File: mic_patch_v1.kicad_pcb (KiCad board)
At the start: 4 copper layers, 40 x 31 mm, 54 parts, among them J1 Conn_ARM_SWD_TagConnect_TC203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, J2 J_000002, J3 J_000001, J4 Micro_SD_Card, J5 J_000003, SW1 SW_000001, SW2 SW_000001, U1 NORA-B106-00B, U2 PWR_nPM1100-QDXX, U3 ADAU7002ACBZ-R7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

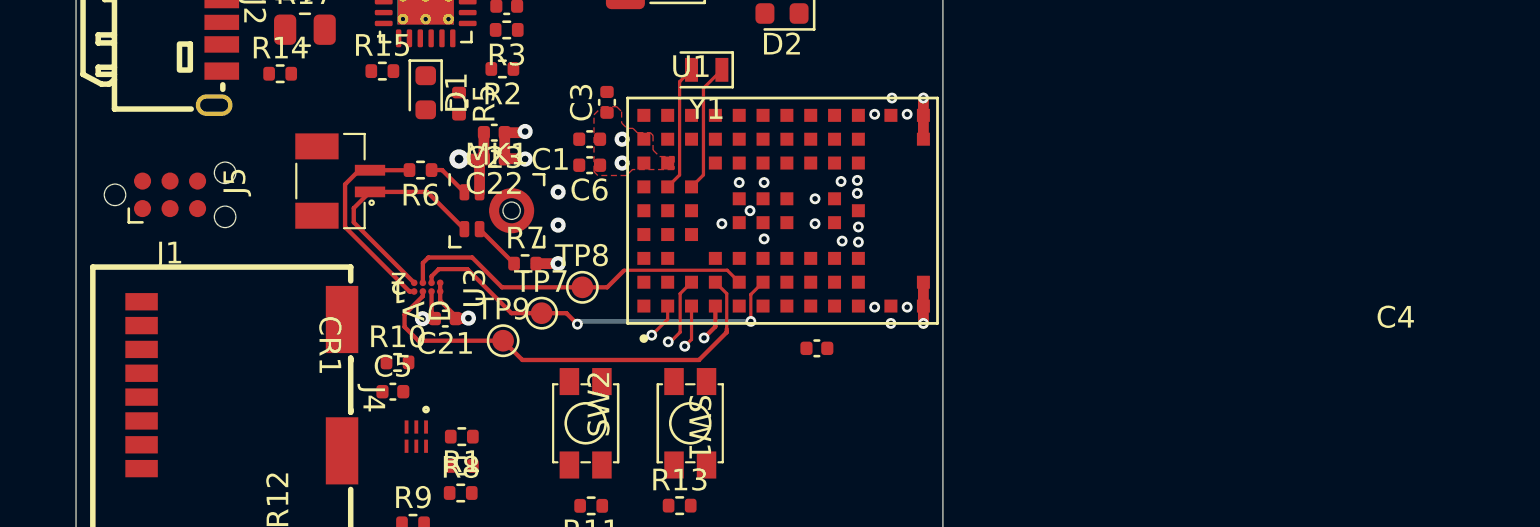
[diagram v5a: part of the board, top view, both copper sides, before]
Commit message: routed SWD/SWO
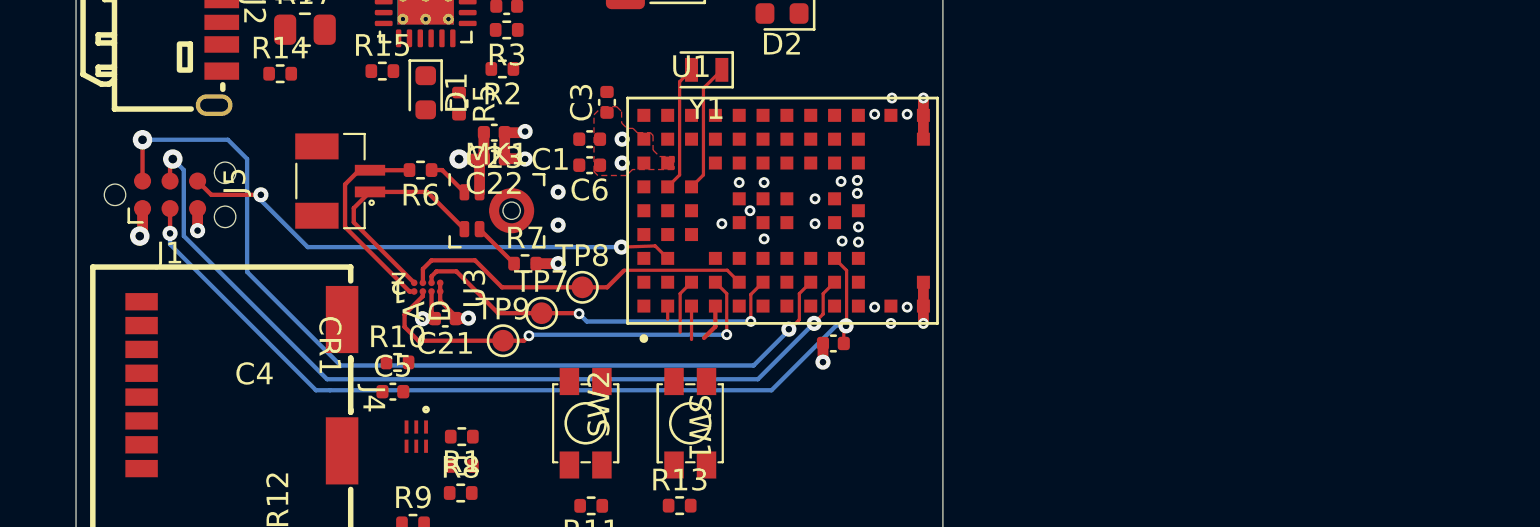
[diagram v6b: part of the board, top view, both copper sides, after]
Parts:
- moved C4 0.79 mm to (164.8, 111.1), turned to 180 degrees
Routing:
- net /MCU/SWDIO: track 0.00 -> 42.4 mm, vias 0 -> 2
- net RESET: track 0.00 -> 41.3 mm, vias 0 -> 2
- net /MCU/SWCLK: track 0.00 -> 40.2 mm, vias 0 -> 2
- net SWO: track 0.00 -> 23.4 mm, vias 0 -> 2
- net GND: track 9.86 -> 11.7 mm, vias 27 -> 29
- net +3V0 VDD_NRF: track 6.57 -> 7.89 mm, vias 4 -> 5
- net SD SCLK: track 1.65 -> 0.61 mm, vias 1 -> 0
- net SD MOSI: track 3.26 -> 2.52 mm, vias 1 -> 0
- net DIN: track 20.5 -> 19.9 mm, vias 0 -> 2
- net SD MISO: track 1.98 -> 1.54 mm, vias 1 -> 0
- net SD CSN: vias 1 -> 0

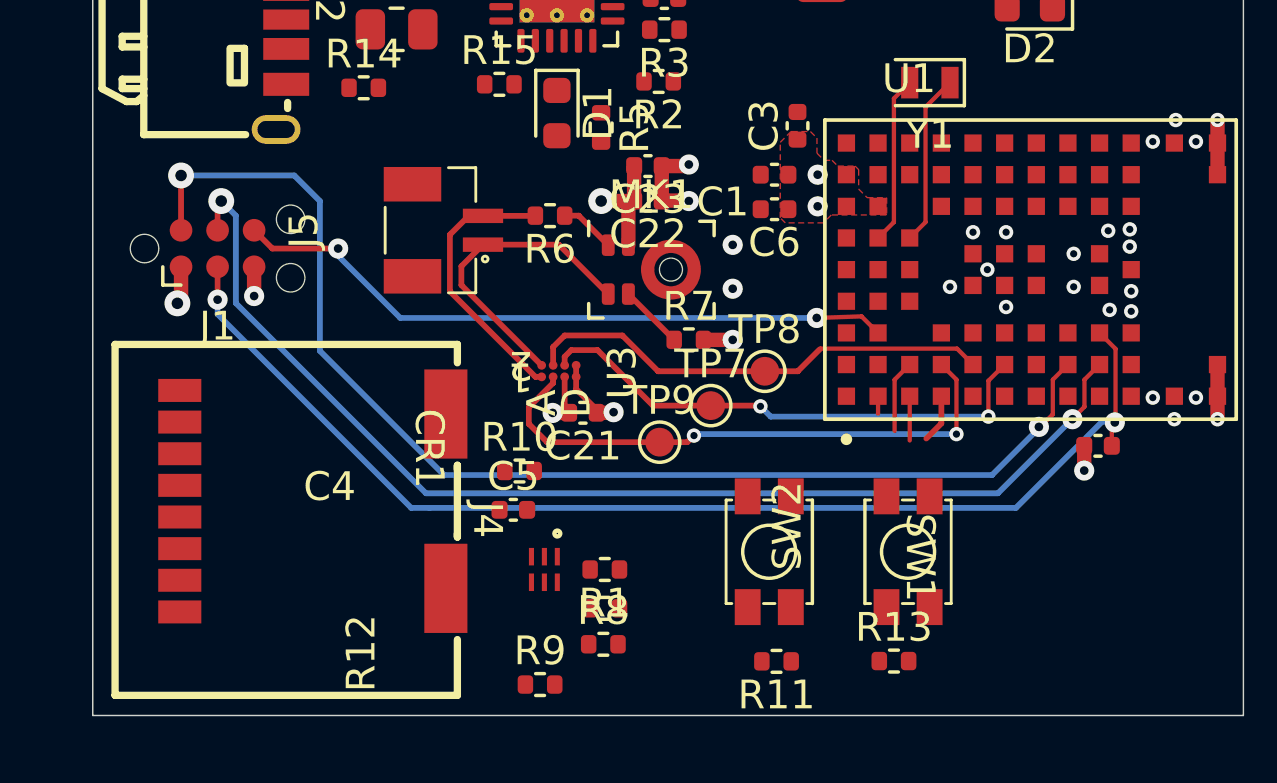
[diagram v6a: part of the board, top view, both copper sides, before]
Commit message: swapped MOSI and MISO pins on SD ESD
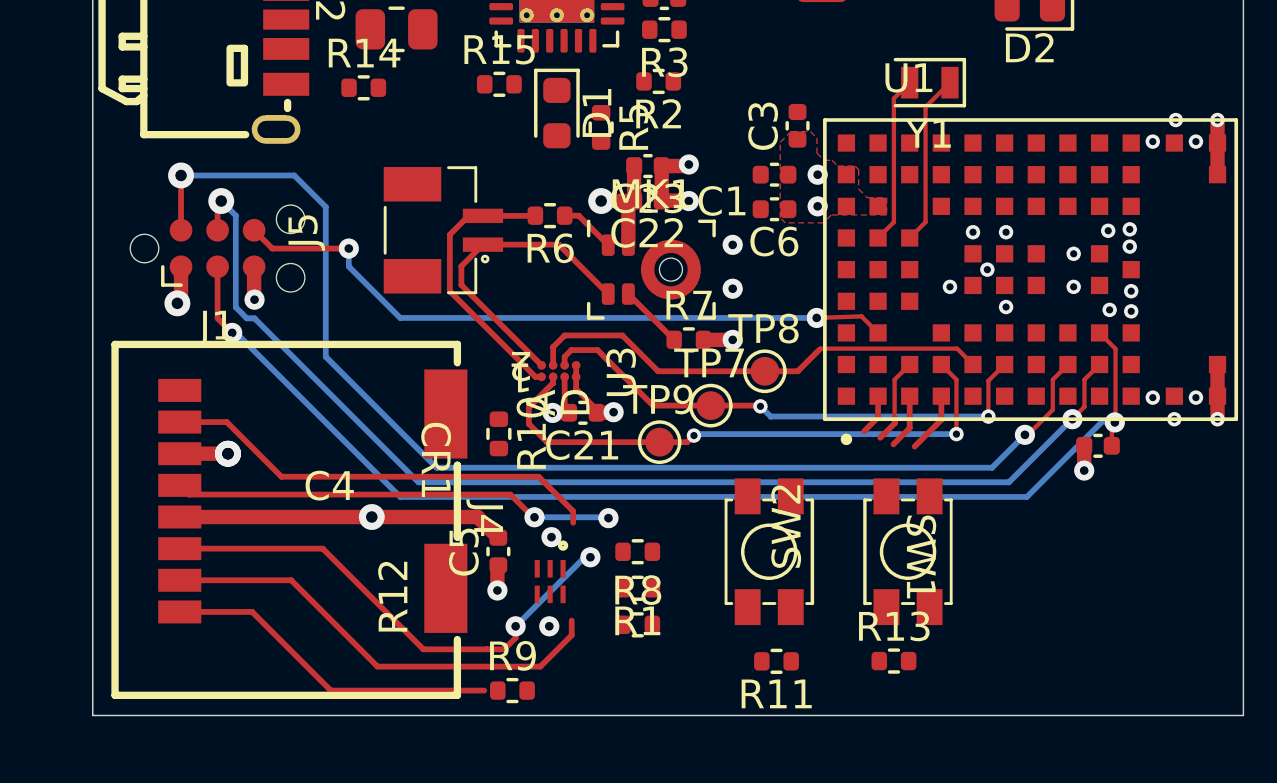
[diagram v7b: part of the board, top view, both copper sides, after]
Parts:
- moved R12 2.27 mm to (148.8, 114.8)
- moved C5 1.54 mm to (144.0, 114.8), turned to 90 degrees
- moved R10 1.48 mm to (144.0, 110.7), turned to -90 degrees
- moved R8 1.37 mm to (148.8, 117.3)
- moved R1 1.32 mm to (148.8, 116.1)
- moved R9 0.98 mm to (144.5, 119.6)
- moved CR1 0.47 mm to (145.8, 115.8)
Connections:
- CR1 pad 4: SD CSN -> SD MOSI
- CR1 pad 6: SD MOSI -> SD CSN
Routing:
- net SD MOSI: track 2.52 -> 20.3 mm, vias 0 -> 2
- net SD CSN: track 1.70 -> 18.0 mm
- net SD SCLK: track 0.61 -> 16.8 mm, vias 0 -> 2
- net SD MISO: track 1.54 -> 17.3 mm
- net /SD_card/DAT_2_pull_up: track 0.00 -> 11.7 mm
- net +3V0 VDD_NRF: track 7.89 -> 19.3 mm, vias 5 -> 6
- net GND: track 11.7 -> 14.4 mm, vias 29 -> 34

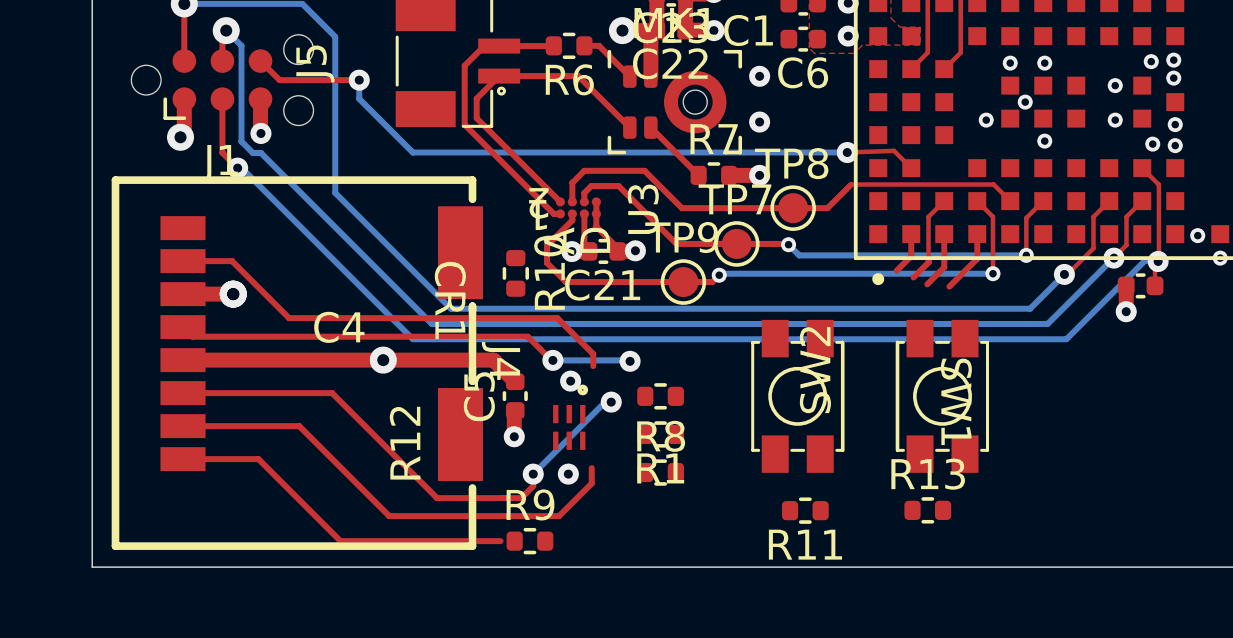
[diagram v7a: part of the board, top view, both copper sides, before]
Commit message: first SD route
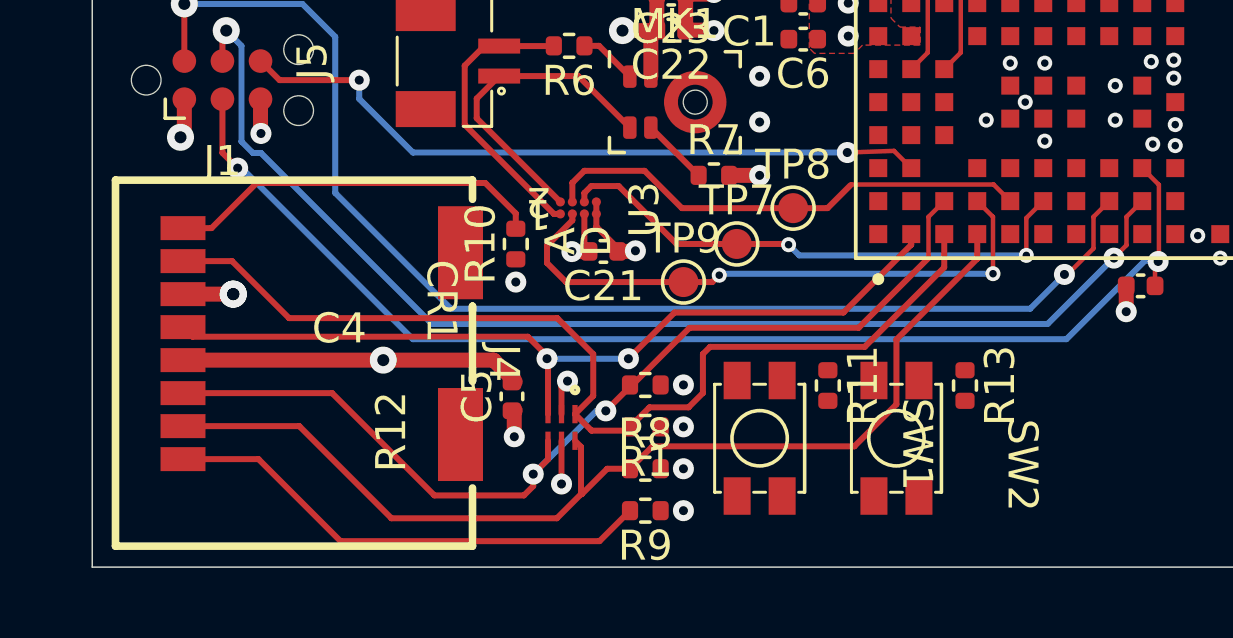
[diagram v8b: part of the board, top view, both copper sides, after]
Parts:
- moved R13 4.34 mm to (159.0, 114.4), turned to -90 degrees
- moved R11 4.24 mm to (154.4, 114.4), turned to -90 degrees
- moved R9 3.98 mm to (148.3, 118.6), turned to 180 degrees
- moved SW2 2.08 mm to (156.7, 116.2), turned to -90 degrees
- moved SW1 1.89 mm to (152.1, 116.2)
- moved R10 0.98 mm to (144.0, 109.7), turned to 90 degrees
- moved R12 0.63 mm to (148.3, 114.4)
- moved R1 0.57 mm to (148.3, 115.8)
- moved R8 0.52 mm to (148.3, 117.2)
- moved CR1 0.26 mm to (145.5, 115.8)
- moved C5 0.11 mm to (143.9, 114.8)
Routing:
- net SD CSN: track 18.0 -> 35.3 mm
- net SD MISO: track 17.3 -> 33.9 mm
- net SD MOSI: track 20.3 -> 33.2 mm
- net /SD_card/DAT1_pull_up: track 0.00 -> 12.6 mm
- net SD SCLK: track 16.8 -> 28.6 mm
- net /SD_card/DAT_2_pull_up: track 11.7 -> 16.5 mm
- net GND: track 14.4 -> 17.1 mm
- net +3V0 VDD_NRF: vias 6 -> 11
